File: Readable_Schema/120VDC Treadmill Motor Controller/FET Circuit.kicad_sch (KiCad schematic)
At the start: 5 parts

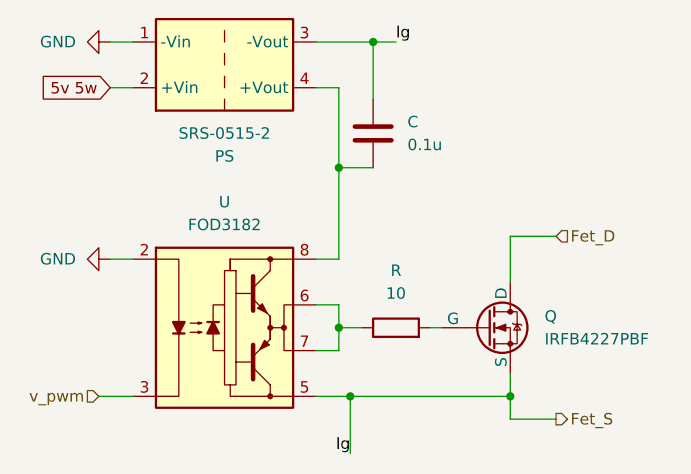
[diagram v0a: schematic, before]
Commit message: I cant for the life of me get the current sensing to actually properly scale with current, I treid 5 different sim models and right now the DA is the best but doesnt start showing anything till around 19amps which kind of defeats the purpose
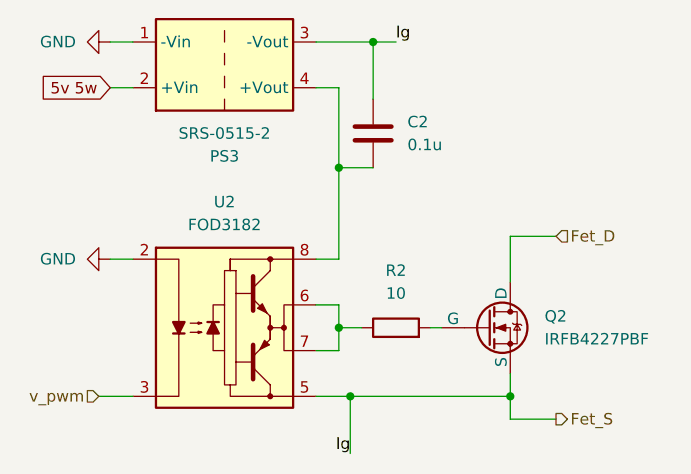
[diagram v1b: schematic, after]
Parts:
- renumbered C to C2, PS to PS3, Q to Q2, R to R2, U to U2
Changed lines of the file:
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@@
 		(on_board yes)
 		(dnp no)
-		(property "Reference" "PS"
+		(property "Reference" "PS?"
 			(at 110.49 73.66 0)
 			(effects
@@
 				(path "/319bc5c0-2dd5-4df3-a34b-9170833ebccd/49a5a11b-8174-445d-b343-1fe5ec8c60de/0ee8c600-4f6e-4877-94f0-4a0da87ba88d"
 					(reference "PS3")
+					(unit 1)
+				)
+				(path "/319bc5c0-2dd5-4df3-a34b-9170833ebccd/49a5a11b-8174-445d-b343-1fe5ec8c60de/3fdd0583-4397-41b2-a5bd-03892cb022fe"
+					(reference "PS2")
+					(unit 1)
+				)
+				(path "/319bc5c0-2dd5-4df3-a34b-9170833ebccd/49a5a11b-8174-445d-b343-1fe5ec8c60de/6d3d8f4c-8a5d-4b0c-94fd-c45e8627b14b"
+					(reference "PS?")
+					(unit 1)
+				)
+				(path "/319bc5c0-2dd5-4df3-a34b-9170833ebccd/49a5a11b-8174-445d-b343-1fe5ec8c60de/ab7f6423-0c29-4aee-927d-1e85ab5c65be"
+					(reference "PS4")
 					(unit 1)
 				)
@@
 		(dnp no)
 		(fields_autoplaced yes)
-		(property "Reference" "#PWR"
+		(property "Reference" "#PWR?"
 			(at 91.44 60.96 0)
 			(effects
@@
 				(path "/319bc5c0-2dd5-4df3-a34b-9170833ebccd/49a5a11b-8174-445d-b343-1fe5ec8c60de/0ee8c600-4f6e-4877-94f0-4a0da87ba88d"
 					(reference "#PWR05")
+					(unit 1)
+				)
+				(path "/319bc5c0-2dd5-4df3-a34b-9170833ebccd/49a5a11b-8174-445d-b343-1fe5ec8c60de/3fdd0583-4397-41b2-a5bd-03892cb022fe"
+					(reference "#PWR04")
+					(unit 1)
+				)
+				(path "/319bc5c0-2dd5-4df3-a34b-9170833ebccd/49a5a11b-8174-445d-b343-1fe5ec8c60de/6d3d8f4c-8a5d-4b0c-94fd-c45e8627b14b"
+					(reference "#PWR?")
+					(unit 1)
+				)
+				(path "/319bc5c0-2dd5-4df3-a34b-9170833ebccd/49a5a11b-8174-445d-b343-1fe5ec8c60de/ab7f6423-0c29-4aee-927d-1e85ab5c65be"
+					(reference "#PWR08")
 					(unit 1)
 				)
@@
 		(dnp no)
 		(fields_autoplaced yes)
-		(property "Reference" "#PWR"
+		(property "Reference" "#PWR?"
 			(at 91.44 85.09 0)
 			(effects
@@
 				(path "/319bc5c0-2dd5-4df3-a34b-9170833ebccd/49a5a11b-8174-445d-b343-1fe5ec8c60de/0ee8c600-4f6e-4877-94f0-4a0da87ba88d"
 					(reference "#PWR06")
+					(unit 1)
+				)
+				(path "/319bc5c0-2dd5-4df3-a34b-9170833ebccd/49a5a11b-8174-445d-b343-1fe5ec8c60de/3fdd0583-4397-41b2-a5bd-03892cb022fe"
+					(reference "#PWR07")
+					(unit 1)
+				)
+				(path "/319bc5c0-2dd5-4df3-a34b-9170833ebccd/49a5a11b-8174-445d-b343-1fe5ec8c60de/6d3d8f4c-8a5d-4b0c-94fd-c45e8627b14b"
+					(reference "#PWR?")
+					(unit 1)
+				)
+				(path "/319bc5c0-2dd5-4df3-a34b-9170833ebccd/49a5a11b-8174-445d-b343-1fe5ec8c60de/ab7f6423-0c29-4aee-927d-1e85ab5c65be"
+					(reference "#PWR09")
 					(unit 1)
 				)
@@
 		(dnp no)
 		(fields_autoplaced yes)
-		(property "Reference" "C"
+		(property "Reference" "C?"
 			(at 130.81 69.8499 0)
 			(effects
@@
 				(path "/319bc5c0-2dd5-4df3-a34b-9170833ebccd/49a5a11b-8174-445d-b343-1fe5ec8c60de/0ee8c600-4f6e-4877-94f0-4a0da87ba88d"
 					(reference "C2")
+					(unit 1)
+				)
+				(path "/319bc5c0-2dd5-4df3-a34b-9170833ebccd/49a5a11b-8174-445d-b343-1fe5ec8c60de/3fdd0583-4397-41b2-a5bd-03892cb022fe"
+					(reference "C1")
+					(unit 1)
+				)
+				(path "/319bc5c0-2dd5-4df3-a34b-9170833ebccd/49a5a11b-8174-445d-b343-1fe5ec8c60de/6d3d8f4c-8a5d-4b0c-94fd-c45e8627b14b"
+					(reference "C?")
+					(unit 1)
+				)
+				(path "/319bc5c0-2dd5-4df3-a34b-9170833ebccd/49a5a11b-8174-445d-b343-1fe5ec8c60de/ab7f6423-0c29-4aee-927d-1e85ab5c65be"
+					(reference "C3")
 					(unit 1)
 				)
@@
 		(dnp no)
 		(fields_autoplaced yes)
-		(property "Reference" "Q"
+		(property "Reference" "Q?"
 			(at 146.05 91.4399 0)
 			(effects
@@
 				(path "/319bc5c0-2dd5-4df3-a34b-9170833ebccd/49a5a11b-8174-445d-b343-1fe5ec8c60de/0ee8c600-4f6e-4877-94f0-4a0da87ba88d"
 					(reference "Q2")
+					(unit 1)
+				)
+				(path "/319bc5c0-2dd5-4df3-a34b-9170833ebccd/49a5a11b-8174-445d-b343-1fe5ec8c60de/3fdd0583-4397-41b2-a5bd-03892cb022fe"
+					(reference "Q1")
+					(unit 1)
+				)
+				(path "/319bc5c0-2dd5-4df3-a34b-9170833ebccd/49a5a11b-8174-445d-b343-1fe5ec8c60de/6d3d8f4c-8a5d-4b0c-94fd-c45e8627b14b"
+					(reference "Q?")
+					(unit 1)
+				)
+				(path "/319bc5c0-2dd5-4df3-a34b-9170833ebccd/49a5a11b-8174-445d-b343-1fe5ec8c60de/ab7f6423-0c29-4aee-927d-1e85ab5c65be"
+					(reference "Q3")
 					(unit 1)
 				)
@@
 		(dnp no)
 		(fields_autoplaced yes)
-		(property "Reference" "R"
+		(property "Reference" "R?"
 			(at 129.54 86.36 90)
 			(effects
@@
 				(path "/319bc5c0-2dd5-4df3-a34b-9170833ebccd/49a5a11b-8174-445d-b343-1fe5ec8c60de/0ee8c600-4f6e-4877-94f0-4a0da87ba88d"
 					(reference "R2")
+					(unit 1)
+				)
+				(path "/319bc5c0-2dd5-4df3-a34b-9170833ebccd/49a5a11b-8174-445d-b343-1fe5ec8c60de/3fdd0583-4397-41b2-a5bd-03892cb022fe"
+					(reference "R1")
+					(unit 1)
+				)
+				(path "/319bc5c0-2dd5-4df3-a34b-9170833ebccd/49a5a11b-8174-445d-b343-1fe5ec8c60de/6d3d8f4c-8a5d-4b0c-94fd-c45e8627b14b"
+					(reference "R?")
+					(unit 1)
+				)
+				(path "/319bc5c0-2dd5-4df3-a34b-9170833ebccd/49a5a11b-8174-445d-b343-1fe5ec8c60de/ab7f6423-0c29-4aee-927d-1e85ab5c65be"
+					(reference "R3")
 					(unit 1)
 				)
@@
 		(dnp no)
 		(fields_autoplaced yes)
-		(property "Reference" "U"
+		(property "Reference" "U?"
 			(at 110.49 78.74 0)
 			(effects
@@
 					(unit 1)
 				)
+				(path "/319bc5c0-2dd5-4df3-a34b-9170833ebccd/49a5a11b-8174-445d-b343-1fe5ec8c60de/3fdd0583-4397-41b2-a5bd-03892cb022fe"
+					(reference "U1")
+					(unit 1)
+				)
+				(path "/319bc5c0-2dd5-4df3-a34b-9170833ebccd/49a5a11b-8174-445d-b343-1fe5ec8c60de/6d3d8f4c-8a5d-4b0c-94fd-c45e8627b14b"
+					(reference "U?")
+					(unit 1)
+				)
+				(path "/319bc5c0-2dd5-4df3-a34b-9170833ebccd/49a5a11b-8174-445d-b343-1fe5ec8c60de/ab7f6423-0c29-4aee-927d-1e85ab5c65be"
+					(reference "U3")
+					(unit 1)
+				)

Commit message: Tried better simulating back emf with little success, started adding footprints and real components to the readable schema (kicad)
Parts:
- Q2: footprint (none) -> Package_TO_SOT_THT:TO-220-3_Vertical
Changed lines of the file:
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@@
 			)
 		)
-		(property "Footprint" ""
+		(property "Footprint" "Package_TO_SOT_THT:TO-220-3_Vertical"
 			(at 144.78 90.17 0)
 			(effects
